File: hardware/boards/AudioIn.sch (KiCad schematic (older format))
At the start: 9 parts, among them J9 AudioJack3_SwitchTR

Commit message: pcb w-i-p
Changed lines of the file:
@@
 $Descr A4 11693 8268
 encoding utf-8
-Sheet 7 8
+Sheet 6 8
 Title ""
 Date ""
@@
 AR Path="/5F6F72DC/5F63C4CD" Ref="R20"  Part="1"
 AR Path="/5F6FD5AE/5F63C4CD" Ref="R24"  Part="1"
-F 0 "R28" H 5620 5696 50  0000 L CNN
+F 0 "R24" H 5620 5696 50  0000 L CNN
 F 1 "100k" H 5620 5605 50  0000 L CNN
 F 2 "Resistor_SMD:R_0805_2012Metric" V 5480 5650 50  0001 C CNN
@@
 AR Path="/5F6F72DC/5F63C4DF" Ref="R22"  Part="1"
 AR Path="/5F6FD5AE/5F63C4DF" Ref="R26"  Part="1"
-F 0 "R30" V 5493 5500 50  0000 C CNN
+F 0 "R26" V 5493 5500 50  0000 C CNN
 F 1 "150" V 5584 5500 50  0000 C CNN
 F 2 "Resistor_SMD:R_0805_2012Metric" V 5630 5500 50  0001 C CNN
@@
 AR Path="/5F6F72DC/5F63C4F5" Ref="C59"  Part="1"
 AR Path="/5F6FD5AE/5F63C4F5" Ref="C63"  Part="1"
-F 0 "C67" H 6265 5696 50  0000 L CNN
+F 0 "C63" H 6265 5696 50  0000 L CNN
 F 1 "2700p" H 6265 5605 50  0000 L CNN
 F 2 "Capacitor_SMD:C_0805_2012Metric" H 6188 5500 50  0001 C CNN
@@
 AR Path="/5F6F72DC/5F63C502" Ref="J7"  Part="1"
 AR Path="/5F6FD5AE/5F63C502" Ref="J8"  Part="1"
-F 0 "J9" H 4020 5325 50  0000 R CNN
+F 0 "J8" H 4020 5325 50  0000 R CNN
 F 1 "AudioJack3_SwitchTR" H 4020 5234 50  0000 R CNN
 F 2 "footprints:ACJS-MV5" H 4300 5400 50  0001 C CNN
@@
 AR Path="/5F6F72DC/5F64573C" Ref="C57"  Part="1"
 AR Path="/5F6FD5AE/5F64573C" Ref="C61"  Part="1"
-F 0 "C65" H 6115 5546 50  0000 L CNN
+F 0 "C61" H 6115 5546 50  0000 L CNN
 F 1 "10u" H 6115 5455 50  0000 L CNN
 F 2 "Capacitor_SMD:C_0805_2012Metric" H 6038 5350 50  0001 C CNN
@@
 AR Path="/5F6F72DC/5F65493E" Ref="R21"  Part="1"
 AR Path="/5F6FD5AE/5F65493E" Ref="R25"  Part="1"
-F 0 "R29" H 5670 4846 50  0000 L CNN
+F 0 "R25" H 5670 4846 50  0000 L CNN
 F 1 "100k" H 5670 4755 50  0000 L CNN
 F 2 "Resistor_SMD:R_0805_2012Metric" V 5530 4800 50  0001 C CNN
@@
 AR Path="/5F6F72DC/5F654944" Ref="R23"  Part="1"
 AR Path="/5F6FD5AE/5F654944" Ref="R27"  Part="1"
-F 0 "R31" V 5543 4650 50  0000 C CNN
+F 0 "R27" V 5543 4650 50  0000 C CNN
 F 1 "150" V 5634 4650 50  0000 C CNN
 F 2 "Resistor_SMD:R_0805_2012Metric" V 5680 4650 50  0001 C CNN
@@
 AR Path="/5F6F72DC/5F65494A" Ref="C60"  Part="1"
 AR Path="/5F6FD5AE/5F65494A" Ref="C64"  Part="1"
-F 0 "C68" H 6315 4846 50  0000 L CNN
+F 0 "C64" H 6315 4846 50  0000 L CNN
 F 1 "2700p" H 6315 4755 50  0000 L CNN
 F 2 "Capacitor_SMD:C_0805_2012Metric" H 6238 4650 50  0001 C CNN
@@
 AR Path="/5F6F72DC/5F654953" Ref="C58"  Part="1"
 AR Path="/5F6FD5AE/5F654953" Ref="C62"  Part="1"
-F 0 "C66" H 6165 4696 50  0000 L CNN
+F 0 "C62" H 6165 4696 50  0000 L CNN
 F 1 "10u" H 6165 4605 50  0000 L CNN
 F 2 "Capacitor_SMD:C_0805_2012Metric" H 6088 4500 50  0001 C CNN

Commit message: wip
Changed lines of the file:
@@
 AR Path="/5F6F72DC/5F63C4CD" Ref="R20"  Part="1"
 AR Path="/5F6FD5AE/5F63C4CD" Ref="R24"  Part="1"
-F 0 "R24" H 5620 5696 50  0000 L CNN
+F 0 "R28" H 5620 5696 50  0000 L CNN
 F 1 "100k" H 5620 5605 50  0000 L CNN
 F 2 "Resistor_SMD:R_0805_2012Metric" V 5480 5650 50  0001 C CNN
@@
 AR Path="/5F6F72DC/5F63C4DF" Ref="R22"  Part="1"
 AR Path="/5F6FD5AE/5F63C4DF" Ref="R26"  Part="1"
-F 0 "R26" V 5493 5500 50  0000 C CNN
+F 0 "R30" V 5493 5500 50  0000 C CNN
 F 1 "150" V 5584 5500 50  0000 C CNN
 F 2 "Resistor_SMD:R_0805_2012Metric" V 5630 5500 50  0001 C CNN
@@
 AR Path="/5F6F72DC/5F63C4F5" Ref="C59"  Part="1"
 AR Path="/5F6FD5AE/5F63C4F5" Ref="C63"  Part="1"
-F 0 "C63" H 6265 5696 50  0000 L CNN
+F 0 "C67" H 6265 5696 50  0000 L CNN
 F 1 "2700p" H 6265 5605 50  0000 L CNN
 F 2 "Capacitor_SMD:C_0805_2012Metric" H 6188 5500 50  0001 C CNN
@@
 AR Path="/5F6F72DC/5F63C502" Ref="J7"  Part="1"
 AR Path="/5F6FD5AE/5F63C502" Ref="J8"  Part="1"
-F 0 "J8" H 4020 5325 50  0000 R CNN
+F 0 "J9" H 4020 5325 50  0000 R CNN
 F 1 "AudioJack3_SwitchTR" H 4020 5234 50  0000 R CNN
 F 2 "footprints:ACJS-MV5" H 4300 5400 50  0001 C CNN
@@
 AR Path="/5F6F72DC/5F64573C" Ref="C57"  Part="1"
 AR Path="/5F6FD5AE/5F64573C" Ref="C61"  Part="1"
-F 0 "C61" H 6115 5546 50  0000 L CNN
+F 0 "C65" H 6115 5546 50  0000 L CNN
 F 1 "10u" H 6115 5455 50  0000 L CNN
 F 2 "Capacitor_SMD:C_0805_2012Metric" H 6038 5350 50  0001 C CNN
@@
 AR Path="/5F6F72DC/5F65493E" Ref="R21"  Part="1"
 AR Path="/5F6FD5AE/5F65493E" Ref="R25"  Part="1"
-F 0 "R25" H 5670 4846 50  0000 L CNN
+F 0 "R29" H 5670 4846 50  0000 L CNN
 F 1 "100k" H 5670 4755 50  0000 L CNN
 F 2 "Resistor_SMD:R_0805_2012Metric" V 5530 4800 50  0001 C CNN
@@
 AR Path="/5F6F72DC/5F654944" Ref="R23"  Part="1"
 AR Path="/5F6FD5AE/5F654944" Ref="R27"  Part="1"
-F 0 "R27" V 5543 4650 50  0000 C CNN
+F 0 "R31" V 5543 4650 50  0000 C CNN
 F 1 "150" V 5634 4650 50  0000 C CNN
 F 2 "Resistor_SMD:R_0805_2012Metric" V 5680 4650 50  0001 C CNN
@@
 AR Path="/5F6F72DC/5F65494A" Ref="C60"  Part="1"
 AR Path="/5F6FD5AE/5F65494A" Ref="C64"  Part="1"
-F 0 "C64" H 6315 4846 50  0000 L CNN
+F 0 "C68" H 6315 4846 50  0000 L CNN
 F 1 "2700p" H 6315 4755 50  0000 L CNN
 F 2 "Capacitor_SMD:C_0805_2012Metric" H 6238 4650 50  0001 C CNN
@@
 AR Path="/5F6F72DC/5F654953" Ref="C58"  Part="1"
 AR Path="/5F6FD5AE/5F654953" Ref="C62"  Part="1"
-F 0 "C62" H 6165 4696 50  0000 L CNN
+F 0 "C66" H 6165 4696 50  0000 L CNN
 F 1 "10u" H 6165 4605 50  0000 L CNN
 F 2 "Capacitor_SMD:C_0805_2012Metric" H 6088 4500 50  0001 C CNN

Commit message: placing imprvmts
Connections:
- net AGND: now also J9.S; no longer J9.T
- net at R28.1, R30.2: now also J9.R; no longer J9.S
- net at R29.1, R31.2: now also J9.T; no longer J9.R
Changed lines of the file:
@@
 $Descr A4 11693 8268
 encoding utf-8
-Sheet 6 8
+Sheet 7 8
 Title ""
 Date ""
@@
 $EndComp
 Wire Wire Line
-	4500 5400 5200 5400
-Wire Wire Line
 	4500 5300 4850 5300
 Wire Wire Line
-	4850 5300 4850 5200
-Wire Wire Line
 	4850 5100 4500 5100
-Wire Wire Line
-	4500 5200 4850 5200
-Connection ~ 4850 5200
-Wire Wire Line
-	4850 5200 4850 5100
 Text HLabel 6650 5500 2    50   Input ~ 0
 LEFT
@@
 Text Label 6150 5800 0    50   ~ 0
 AGND
-Wire Wire Line
-	4500 5500 5550 5500
-Connection ~ 5550 5500
 $Comp
 L Device:C C?
@@
 Connection ~ 6200 4650
 Wire Wire Line
-	5200 5400 5200 4650
-Wire Wire Line
 	5200 4650 5600 4650
 Connection ~ 5600 4650
@@
 Wire Wire Line
 	7250 5050 7500 5050
+Text Label 4500 5500 0    50   ~ 0
+AGND
+Text Label 4850 5300 0    50   ~ 0
+AGND
+Wire Wire Line
+	5550 5500 5200 5500
+Connection ~ 5550 5500
+Wire Wire Line
+	5200 5200 5200 4650
+Wire Wire Line
+	4500 5200 5200 5200
+Wire Wire Line
+	5200 5400 5200 5500
+Wire Wire Line
+	4500 5400 5200 5400
 $EndSCHEMATC

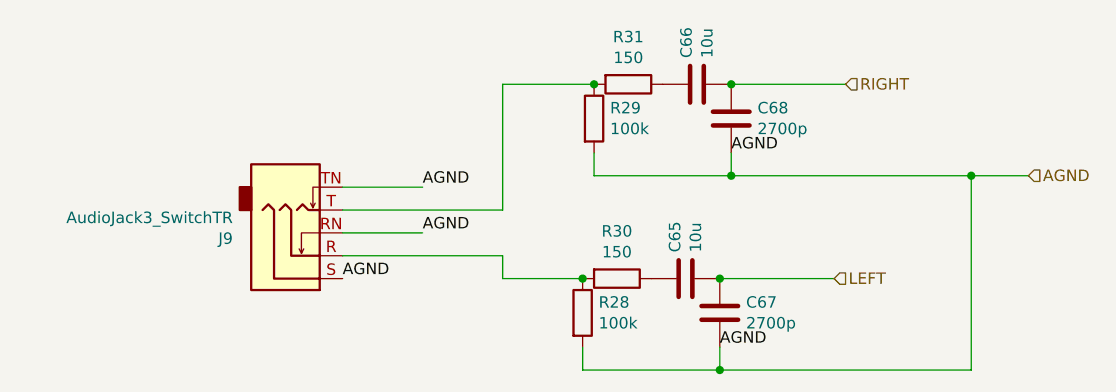
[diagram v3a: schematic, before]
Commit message: mainboard passes drc
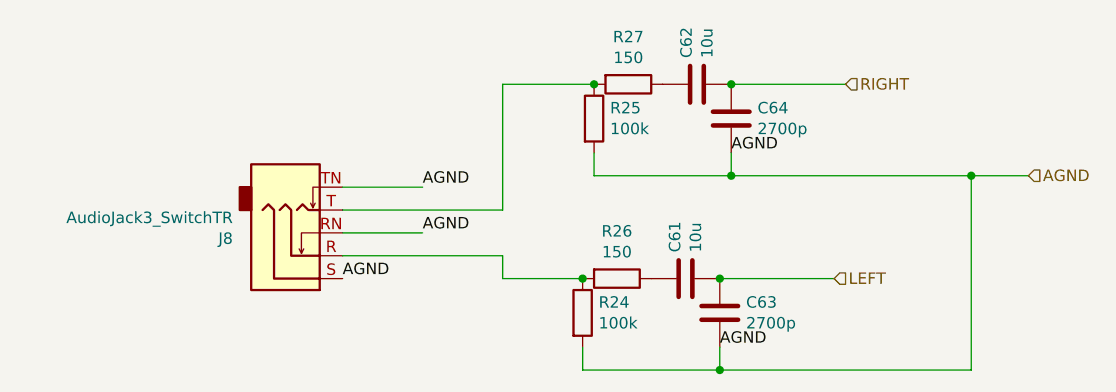
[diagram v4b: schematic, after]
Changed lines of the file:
@@
 $Descr A4 11693 8268
 encoding utf-8
-Sheet 7 8
+Sheet 6 8
 Title ""
 Date ""
@@
 AR Path="/5F6F72DC/5F63C4CD" Ref="R20"  Part="1"
 AR Path="/5F6FD5AE/5F63C4CD" Ref="R24"  Part="1"
-F 0 "R28" H 5620 5696 50  0000 L CNN
+F 0 "R24" H 5620 5696 50  0000 L CNN
 F 1 "100k" H 5620 5605 50  0000 L CNN
 F 2 "Resistor_SMD:R_0805_2012Metric" V 5480 5650 50  0001 C CNN
@@
 AR Path="/5F6F72DC/5F63C4DF" Ref="R22"  Part="1"
 AR Path="/5F6FD5AE/5F63C4DF" Ref="R26"  Part="1"
-F 0 "R30" V 5493 5500 50  0000 C CNN
+F 0 "R26" V 5493 5500 50  0000 C CNN
 F 1 "150" V 5584 5500 50  0000 C CNN
 F 2 "Resistor_SMD:R_0805_2012Metric" V 5630 5500 50  0001 C CNN
@@
 AR Path="/5F6F72DC/5F63C4F5" Ref="C59"  Part="1"
 AR Path="/5F6FD5AE/5F63C4F5" Ref="C63"  Part="1"
-F 0 "C67" H 6265 5696 50  0000 L CNN
+F 0 "C63" H 6265 5696 50  0000 L CNN
 F 1 "2700p" H 6265 5605 50  0000 L CNN
 F 2 "Capacitor_SMD:C_0805_2012Metric" H 6188 5500 50  0001 C CNN
@@
 AR Path="/5F6F72DC/5F63C502" Ref="J7"  Part="1"
 AR Path="/5F6FD5AE/5F63C502" Ref="J8"  Part="1"
-F 0 "J9" H 4020 5325 50  0000 R CNN
+F 0 "J8" H 4020 5325 50  0000 R CNN
 F 1 "AudioJack3_SwitchTR" H 4020 5234 50  0000 R CNN
 F 2 "footprints:ACJS-MV5" H 4300 5400 50  0001 C CNN
@@
 AR Path="/5F6F72DC/5F64573C" Ref="C57"  Part="1"
 AR Path="/5F6FD5AE/5F64573C" Ref="C61"  Part="1"
-F 0 "C65" H 6115 5546 50  0000 L CNN
+F 0 "C61" H 6115 5546 50  0000 L CNN
 F 1 "10u" H 6115 5455 50  0000 L CNN
 F 2 "Capacitor_SMD:C_0805_2012Metric" H 6038 5350 50  0001 C CNN
@@
 AR Path="/5F6F72DC/5F65493E" Ref="R21"  Part="1"
 AR Path="/5F6FD5AE/5F65493E" Ref="R25"  Part="1"
-F 0 "R29" H 5670 4846 50  0000 L CNN
+F 0 "R25" H 5670 4846 50  0000 L CNN
 F 1 "100k" H 5670 4755 50  0000 L CNN
 F 2 "Resistor_SMD:R_0805_2012Metric" V 5530 4800 50  0001 C CNN
@@
 AR Path="/5F6F72DC/5F654944" Ref="R23"  Part="1"
 AR Path="/5F6FD5AE/5F654944" Ref="R27"  Part="1"
-F 0 "R31" V 5543 4650 50  0000 C CNN
+F 0 "R27" V 5543 4650 50  0000 C CNN
 F 1 "150" V 5634 4650 50  0000 C CNN
 F 2 "Resistor_SMD:R_0805_2012Metric" V 5680 4650 50  0001 C CNN
@@
 AR Path="/5F6F72DC/5F65494A" Ref="C60"  Part="1"
 AR Path="/5F6FD5AE/5F65494A" Ref="C64"  Part="1"
-F 0 "C68" H 6315 4846 50  0000 L CNN
+F 0 "C64" H 6315 4846 50  0000 L CNN
 F 1 "2700p" H 6315 4755 50  0000 L CNN
 F 2 "Capacitor_SMD:C_0805_2012Metric" H 6238 4650 50  0001 C CNN
@@
 AR Path="/5F6F72DC/5F654953" Ref="C58"  Part="1"
 AR Path="/5F6FD5AE/5F654953" Ref="C62"  Part="1"
-F 0 "C66" H 6165 4696 50  0000 L CNN
+F 0 "C62" H 6165 4696 50  0000 L CNN
 F 1 "10u" H 6165 4605 50  0000 L CNN
 F 2 "Capacitor_SMD:C_0805_2012Metric" H 6088 4500 50  0001 C CNN

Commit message: Breakout: changed from 4 layer to 2 layer; Mainboard: add serial daisy chain RX/TX to RX4/TX4
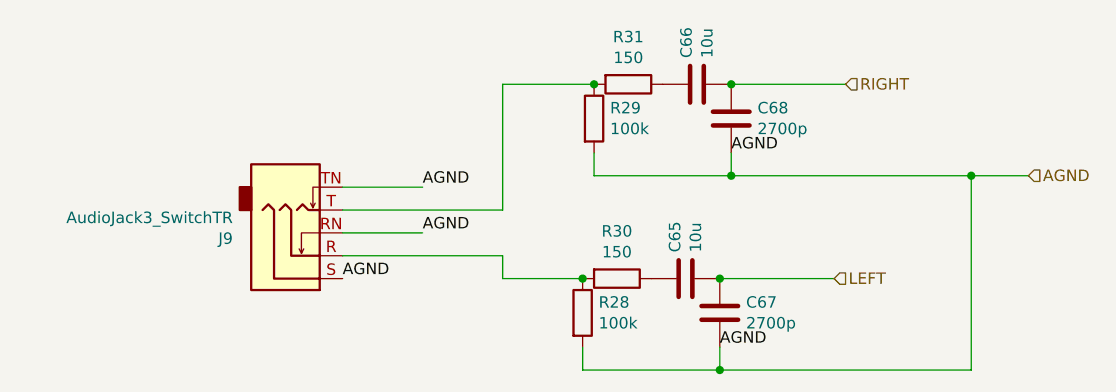
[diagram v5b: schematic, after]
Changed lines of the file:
@@
 AR Path="/5F6F72DC/5F63C4CD" Ref="R20"  Part="1"
 AR Path="/5F6FD5AE/5F63C4CD" Ref="R24"  Part="1"
-F 0 "R24" H 5620 5696 50  0000 L CNN
+F 0 "R28" H 5620 5696 50  0000 L CNN
 F 1 "100k" H 5620 5605 50  0000 L CNN
 F 2 "Resistor_SMD:R_0805_2012Metric" V 5480 5650 50  0001 C CNN
@@
 AR Path="/5F6F72DC/5F63C4DF" Ref="R22"  Part="1"
 AR Path="/5F6FD5AE/5F63C4DF" Ref="R26"  Part="1"
-F 0 "R26" V 5493 5500 50  0000 C CNN
+F 0 "R30" V 5493 5500 50  0000 C CNN
 F 1 "150" V 5584 5500 50  0000 C CNN
 F 2 "Resistor_SMD:R_0805_2012Metric" V 5630 5500 50  0001 C CNN
@@
 AR Path="/5F6F72DC/5F63C4F5" Ref="C59"  Part="1"
 AR Path="/5F6FD5AE/5F63C4F5" Ref="C63"  Part="1"
-F 0 "C63" H 6265 5696 50  0000 L CNN
+F 0 "C67" H 6265 5696 50  0000 L CNN
 F 1 "2700p" H 6265 5605 50  0000 L CNN
 F 2 "Capacitor_SMD:C_0805_2012Metric" H 6188 5500 50  0001 C CNN
@@
 AR Path="/5F6F72DC/5F63C502" Ref="J7"  Part="1"
 AR Path="/5F6FD5AE/5F63C502" Ref="J8"  Part="1"
-F 0 "J8" H 4020 5325 50  0000 R CNN
+F 0 "J9" H 4020 5325 50  0000 R CNN
 F 1 "AudioJack3_SwitchTR" H 4020 5234 50  0000 R CNN
 F 2 "footprints:ACJS-MV5" H 4300 5400 50  0001 C CNN
@@
 AR Path="/5F6F72DC/5F64573C" Ref="C57"  Part="1"
 AR Path="/5F6FD5AE/5F64573C" Ref="C61"  Part="1"
-F 0 "C61" H 6115 5546 50  0000 L CNN
+F 0 "C65" H 6115 5546 50  0000 L CNN
 F 1 "10u" H 6115 5455 50  0000 L CNN
 F 2 "Capacitor_SMD:C_0805_2012Metric" H 6038 5350 50  0001 C CNN
@@
 AR Path="/5F6F72DC/5F65493E" Ref="R21"  Part="1"
 AR Path="/5F6FD5AE/5F65493E" Ref="R25"  Part="1"
-F 0 "R25" H 5670 4846 50  0000 L CNN
+F 0 "R29" H 5670 4846 50  0000 L CNN
 F 1 "100k" H 5670 4755 50  0000 L CNN
 F 2 "Resistor_SMD:R_0805_2012Metric" V 5530 4800 50  0001 C CNN
@@
 AR Path="/5F6F72DC/5F654944" Ref="R23"  Part="1"
 AR Path="/5F6FD5AE/5F654944" Ref="R27"  Part="1"
-F 0 "R27" V 5543 4650 50  0000 C CNN
+F 0 "R31" V 5543 4650 50  0000 C CNN
 F 1 "150" V 5634 4650 50  0000 C CNN
 F 2 "Resistor_SMD:R_0805_2012Metric" V 5680 4650 50  0001 C CNN
@@
 AR Path="/5F6F72DC/5F65494A" Ref="C60"  Part="1"
 AR Path="/5F6FD5AE/5F65494A" Ref="C64"  Part="1"
-F 0 "C64" H 6315 4846 50  0000 L CNN
+F 0 "C68" H 6315 4846 50  0000 L CNN
 F 1 "2700p" H 6315 4755 50  0000 L CNN
 F 2 "Capacitor_SMD:C_0805_2012Metric" H 6238 4650 50  0001 C CNN
@@
 AR Path="/5F6F72DC/5F654953" Ref="C58"  Part="1"
 AR Path="/5F6FD5AE/5F654953" Ref="C62"  Part="1"
-F 0 "C62" H 6165 4696 50  0000 L CNN
+F 0 "C66" H 6165 4696 50  0000 L CNN
 F 1 "10u" H 6165 4605 50  0000 L CNN
 F 2 "Capacitor_SMD:C_0805_2012Metric" H 6088 4500 50  0001 C CNN
